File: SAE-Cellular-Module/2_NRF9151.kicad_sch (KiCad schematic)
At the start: 51 parts, among them J2 MM8130-2600, J3 SWD, Q1 PMOS, Q2 NMOS, Q3 NMOS, Q4 NMOS, Q5 NMOS, SW1 PTS810_SJM_250_SMTR_LFS, SW2 PTS810_SJM_250_SMTR_LFS, U1 NRF9151-LACA-R

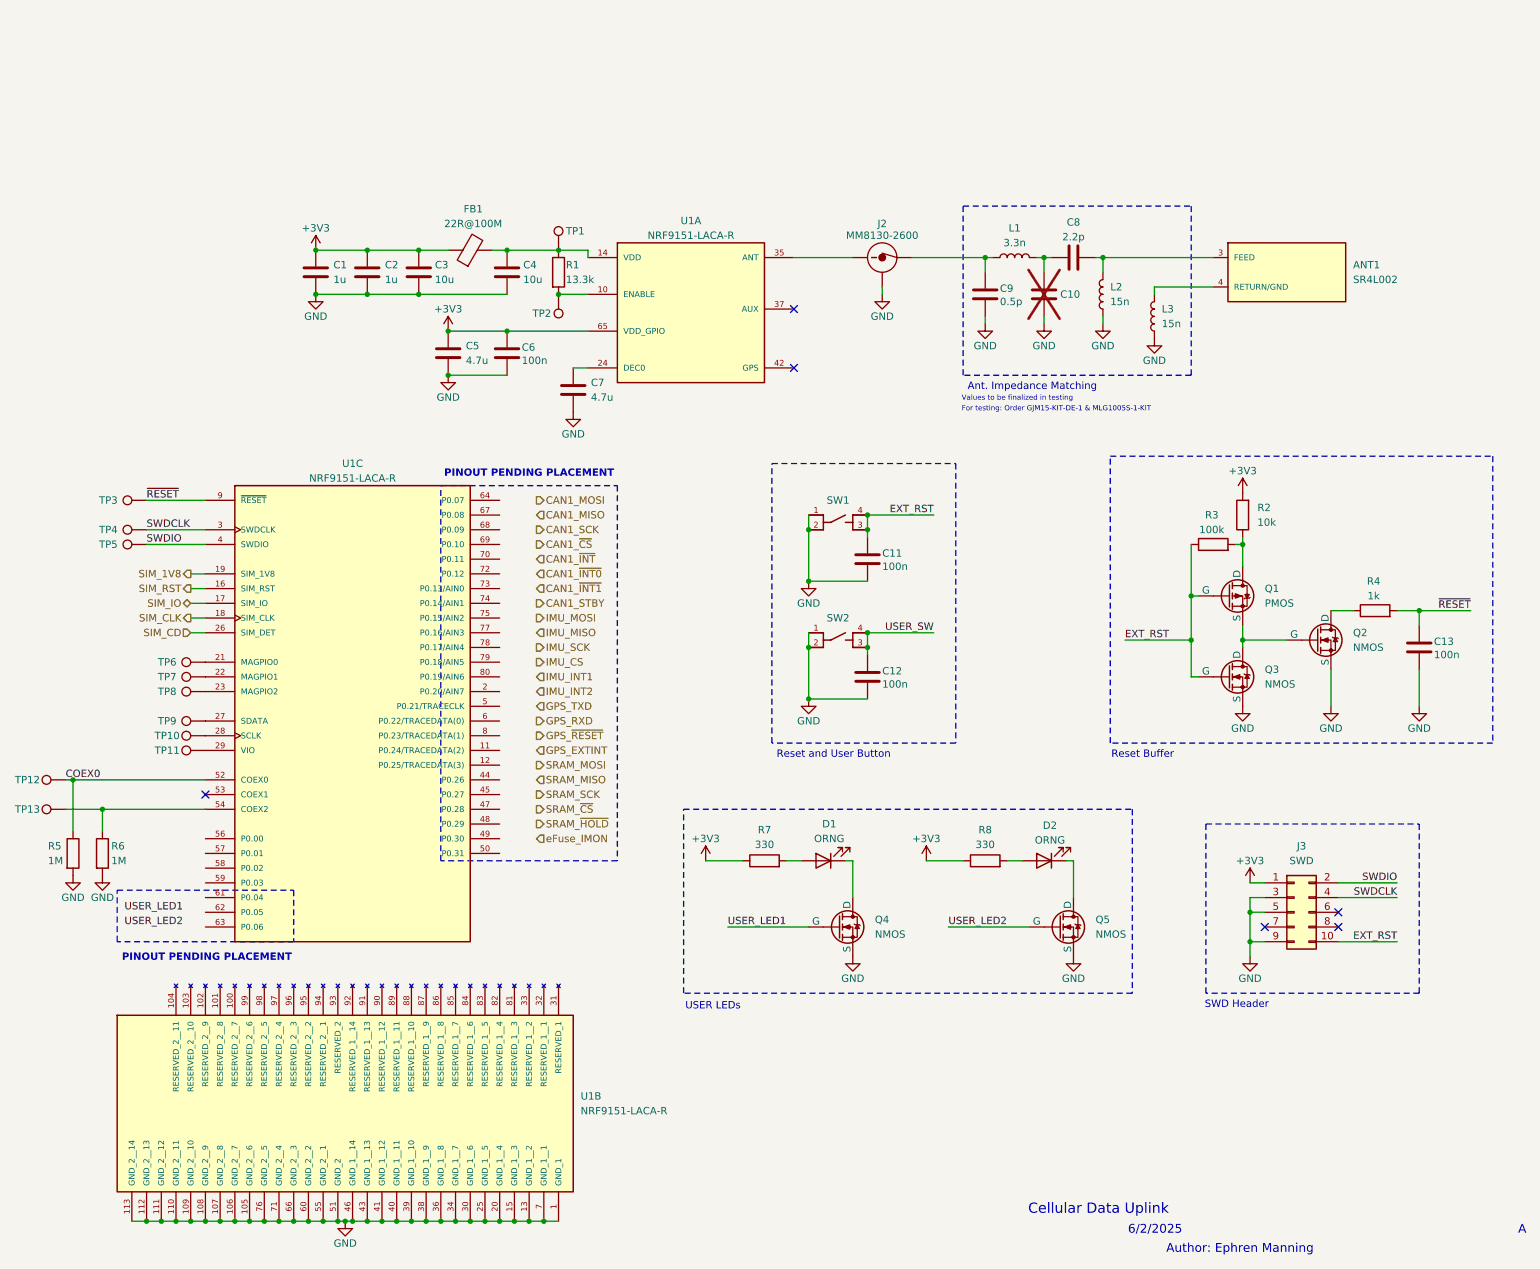
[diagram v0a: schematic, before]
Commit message: Added initial component placements
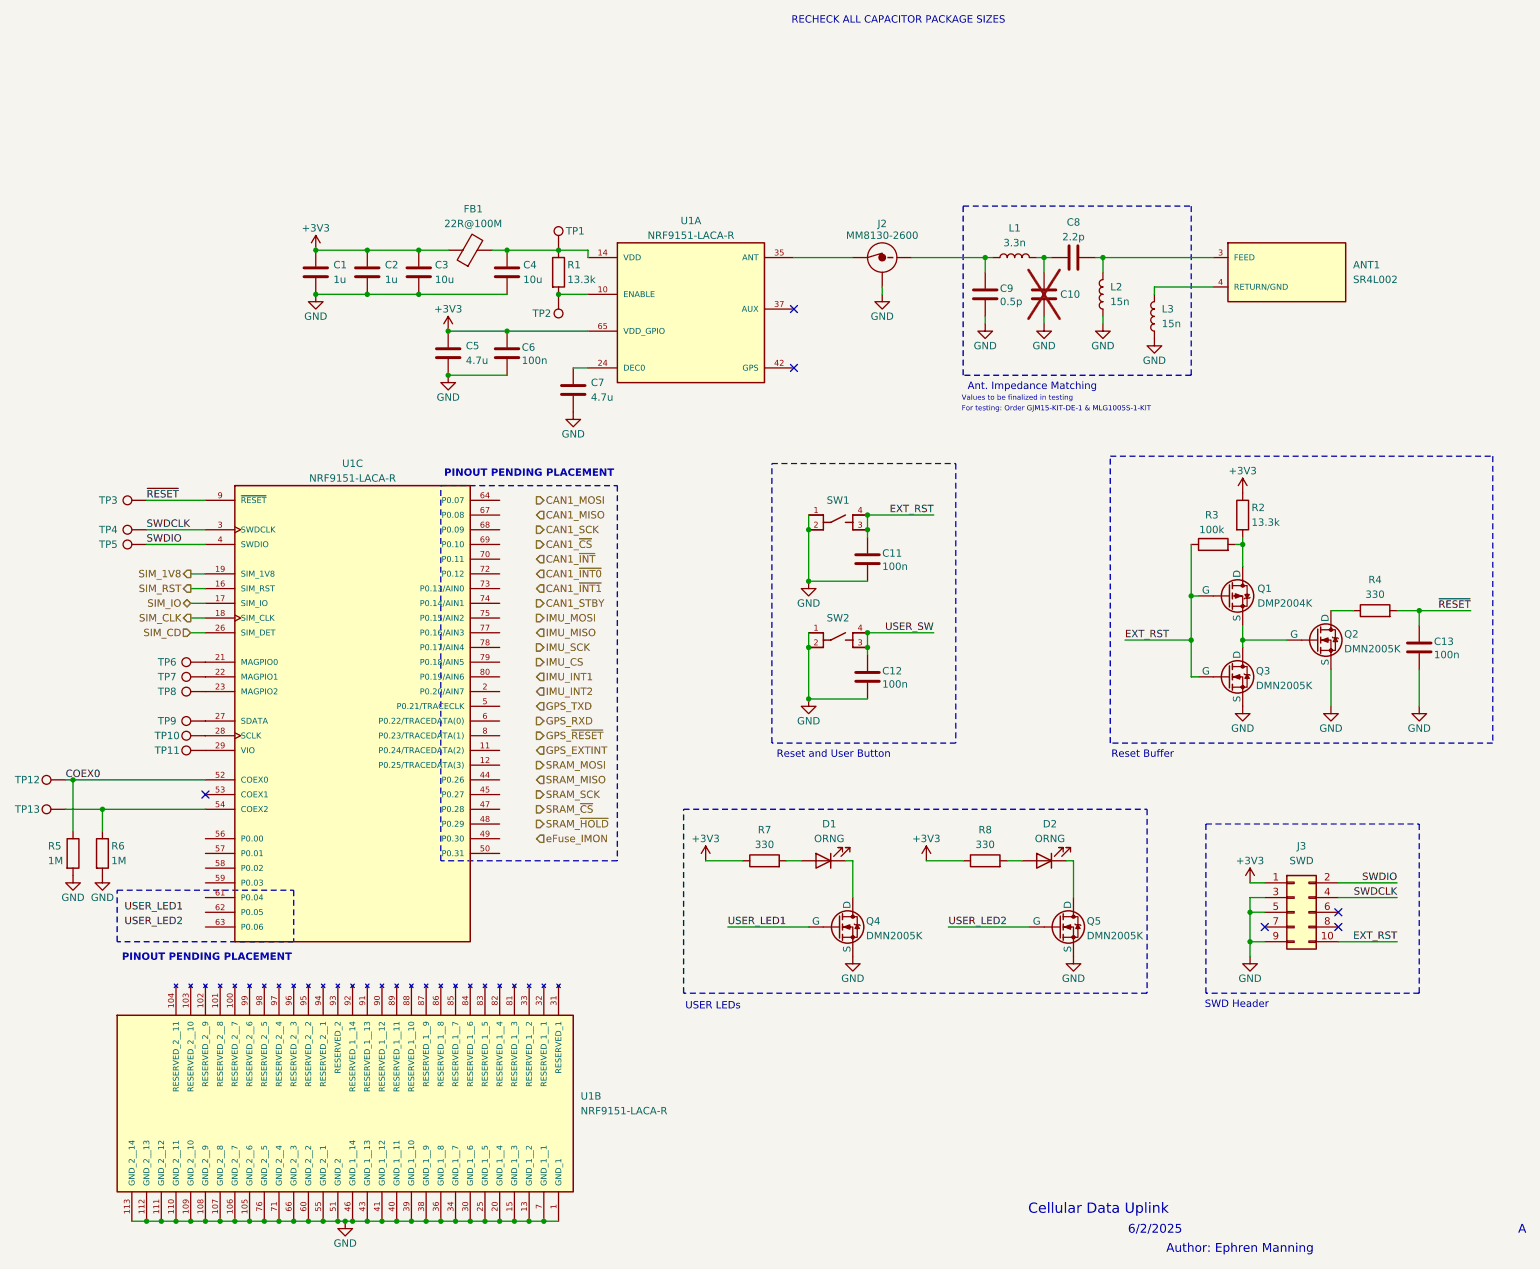
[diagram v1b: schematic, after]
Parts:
- ANT1: MPN (none) -> SR4L002
- C10: value C -> ~
- C5, C7: footprint Capacitor_SMD:C_0805_2012Metric -> Capacitor_SMD:C_0603_1608Metric; MPN CL21A475KPFNNNE -> CL10A475KP8NNNC
- D1, D2: footprint (none) -> LED_SMD:LED_0603_1608Metric; MPN (none) -> 150060AS75000
- J2: footprint MM8130-2600:MURATA_MM8130-2600RA2 -> MM8130_2600RA2:MURATA_MM8130-2600RA2; MPN (none) -> MM8130-2600RA2
- J3: footprint (none) -> Connector_PinHeader_1.27mm:PinHeader_2x05_P1.27mm_Vertical; MPN (none) -> PRPC005DFAN-RC
- Q1: value PMOS -> DMP2004K; footprint (none) -> Package_TO_SOT_SMD:SOT-23-3; MPN (none) -> DMP2004K-7
- Q2, Q3, Q4, Q5: value NMOS -> DMN2005K; footprint (none) -> Package_TO_SOT_SMD:SOT-23-3; MPN (none) -> DMN2005K-7
- R1: footprint (none) -> Resistor_SMD:R_0402_1005Metric; MPN (none) -> ERJ-2RKF1332X
- R2: value 10k -> 13.3k; footprint (none) -> Resistor_SMD:R_0402_1005Metric; MPN (none) -> ERJ-2RKF1332X
- R3: footprint (none) -> Resistor_SMD:R_0402_1005Metric; MPN (none) -> ERJ-2RKF1003X
- R4: value 1k -> 330; footprint (none) -> Resistor_SMD:R_0402_1005Metric; MPN (none) -> ERJ-2RKF3300X
- R5, R6: footprint (none) -> Resistor_SMD:R_0402_1005Metric; MPN (none) -> RC0402FR-071ML
- R7, R8: footprint (none) -> Resistor_SMD:R_0402_1005Metric; MPN (none) -> ERJ-2RKF3300X
- TP1, TP10, TP11, TP12, TP13, TP2, TP3, TP4, TP5, TP6, TP7, TP8, TP9: footprint (none) -> TestPoint:TestPoint_Pad_D1.0mm
- U1: footprint NRF9151-LACA-R:XCVR_NRF9151-LACA-R -> NRF9151_LACA_R:XCVR_NRF9151-LACA-R
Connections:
- net +3V3: now also R2.1; no longer R2.2
- net at Q1.1 (D), R3.2: now also R2.2; no longer R2.1
- net at C9.2, L1.1: now also J2.IN; no longer J2.OUT
- net at U1.35 (ANT): now also J2.OUT; no longer J2.IN
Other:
- note added: "RECHECK ALL CAPACITOR PACKAGE SIZES"
